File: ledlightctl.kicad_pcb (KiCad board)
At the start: 2 copper layers, 25 x 20 mm, 8 parts, among them U2 AL8860Q

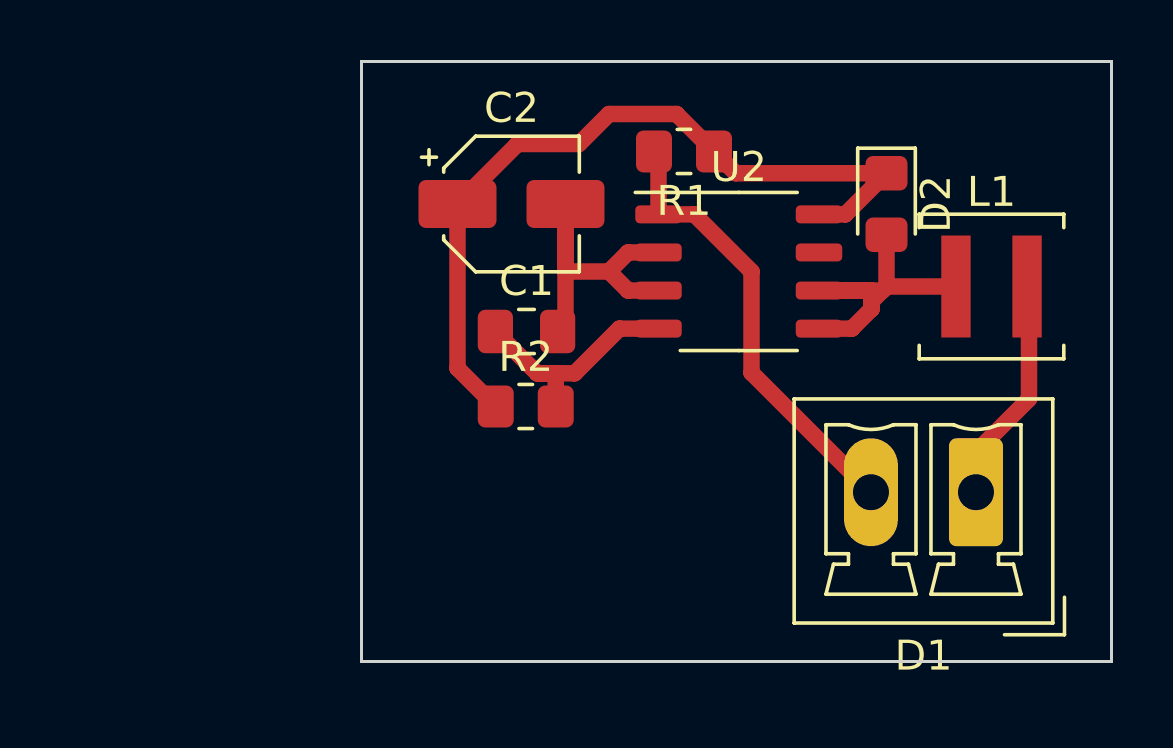
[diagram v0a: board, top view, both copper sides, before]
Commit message: Add GND copper pour
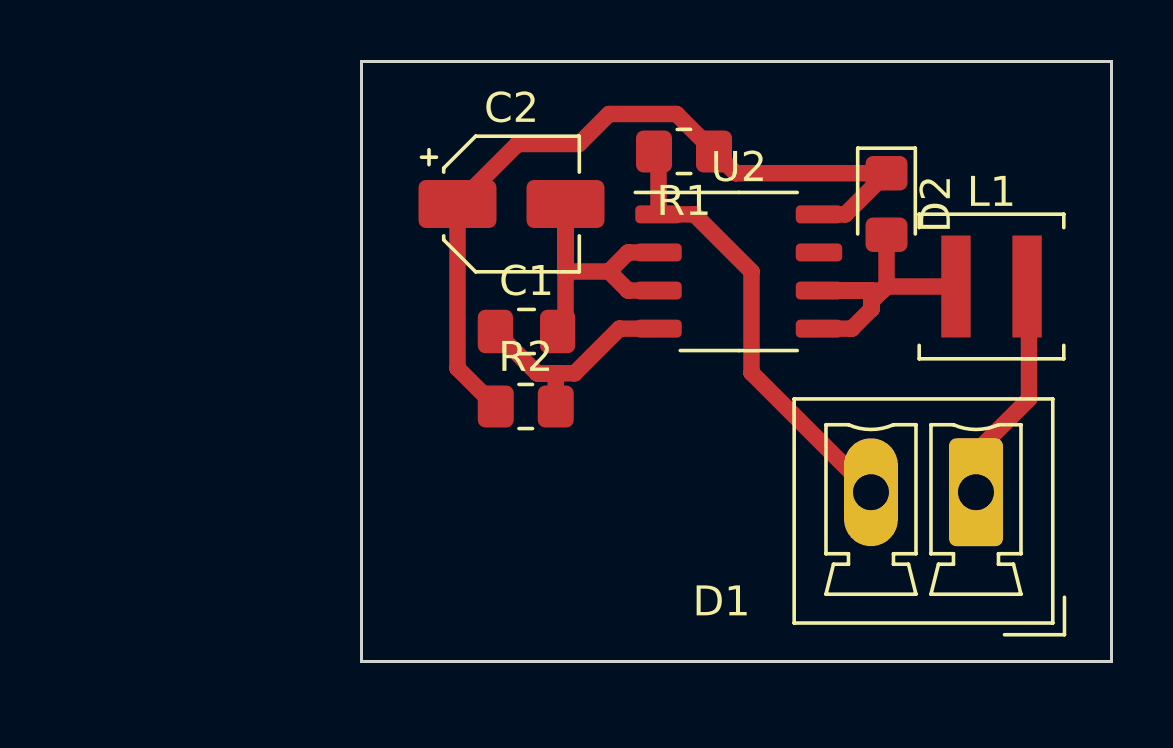
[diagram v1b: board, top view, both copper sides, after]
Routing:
- added copper zone on B.Cu, net GND
- added copper zone on F.Cu, net GND
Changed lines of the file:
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@@
     (property "ki_keywords" "LED diode")
     (attr through_hole)
-    (fp_text reference "D1" (at 1.75 -5.45) (layer "F.SilkS")
+    (fp_text reference "D1" (at 8.4825 -3.6425) (layer "F.SilkS")
         (effects (font (size 1 1) (thickness 0.15)))
     )
@@
   (segment (start 63.5 32.5) (end 65.815 32.5) (width 0.55) (layer "F.Cu") (net 6))
   (segment (start 61.25 33.905) (end 62.345 33.905) (width 0.55) (layer "F.Cu") (net 6))
+  (zone (net 2) (net_name "GND") (layers "F&B.Cu") (hatch edge 0.5)
+    (priority 1)
+    (connect_pads (clearance 0.5))
+    (min_thickness 0.25) (filled_areas_thickness no)
+    (fill (thermal_gap 0.5) (thermal_bridge_width 0.5))
+    (polygon
+      (pts
+        (xy 46 25)
+        (xy 71 25)
+        (xy 71 45)
+        (xy 46 45)
+      )
+    )
+  )
 )

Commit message: Add power connector Add copper zones
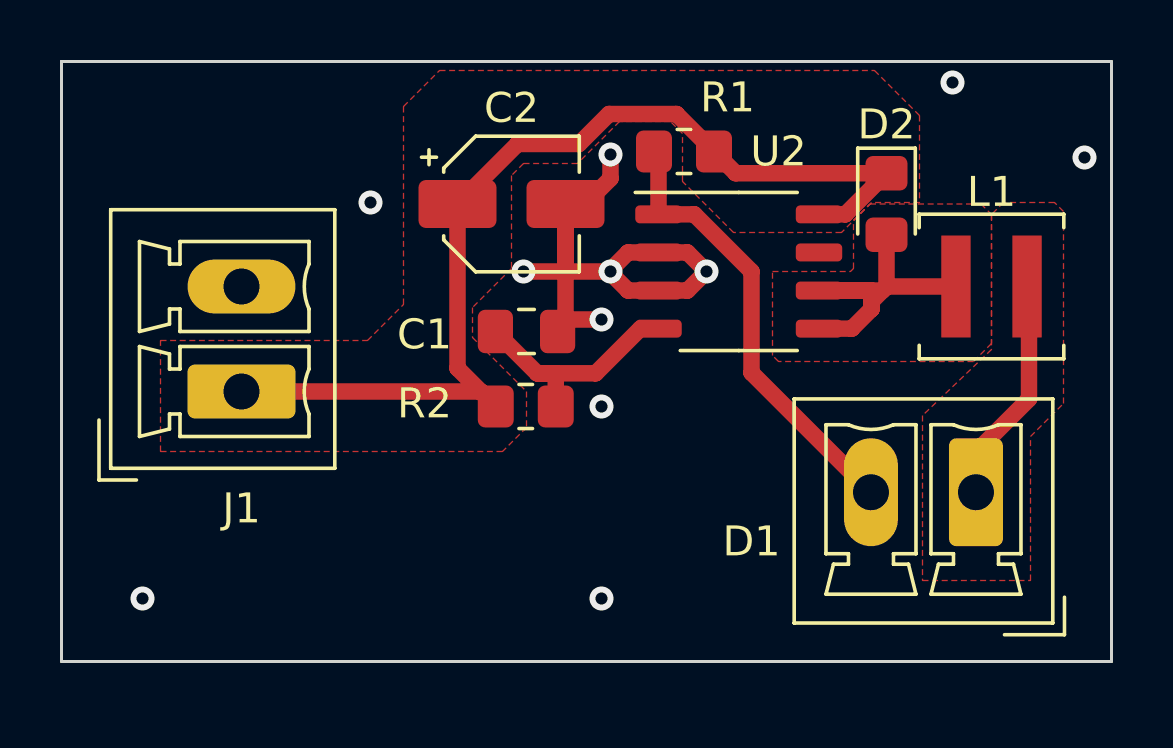
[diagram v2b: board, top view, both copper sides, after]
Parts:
- added J1: Power, Connector_Phoenix_MC:PhoenixContact_MCV_1,5_2-G-3.5_1x02_P3.50mm_Vertical, F.Cu at (42.0, 36.0)
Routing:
- net GND: track 11.9 -> 21.3 mm, vias 0 -> 11
- net +12V: track 26.5 -> 35.1 mm
- added copper zone on F.Cu, net +12V
- added copper zone on F.Cu, net Net-(D1-K)
- added copper zone on F.Cu, net Net-(D2-A)
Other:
- board size 25 x 20 mm -> 35 x 20 mm
